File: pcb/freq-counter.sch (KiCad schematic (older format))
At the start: 52 parts, among them J1 RPM, J2 BNC, J3 for RPM, Q1 CSC388A, Q2 CSC388A, Q3 2SA1015, Q4 2SC1815, Q5 2SC1815, SW1 SW_SPDT, SW2 SW_Push, SW3 SW_Push, U1 SN74HC02N, U2 ATTINY4313-PU(freq-counter), U3 EE-SX460, Y1 10MHz

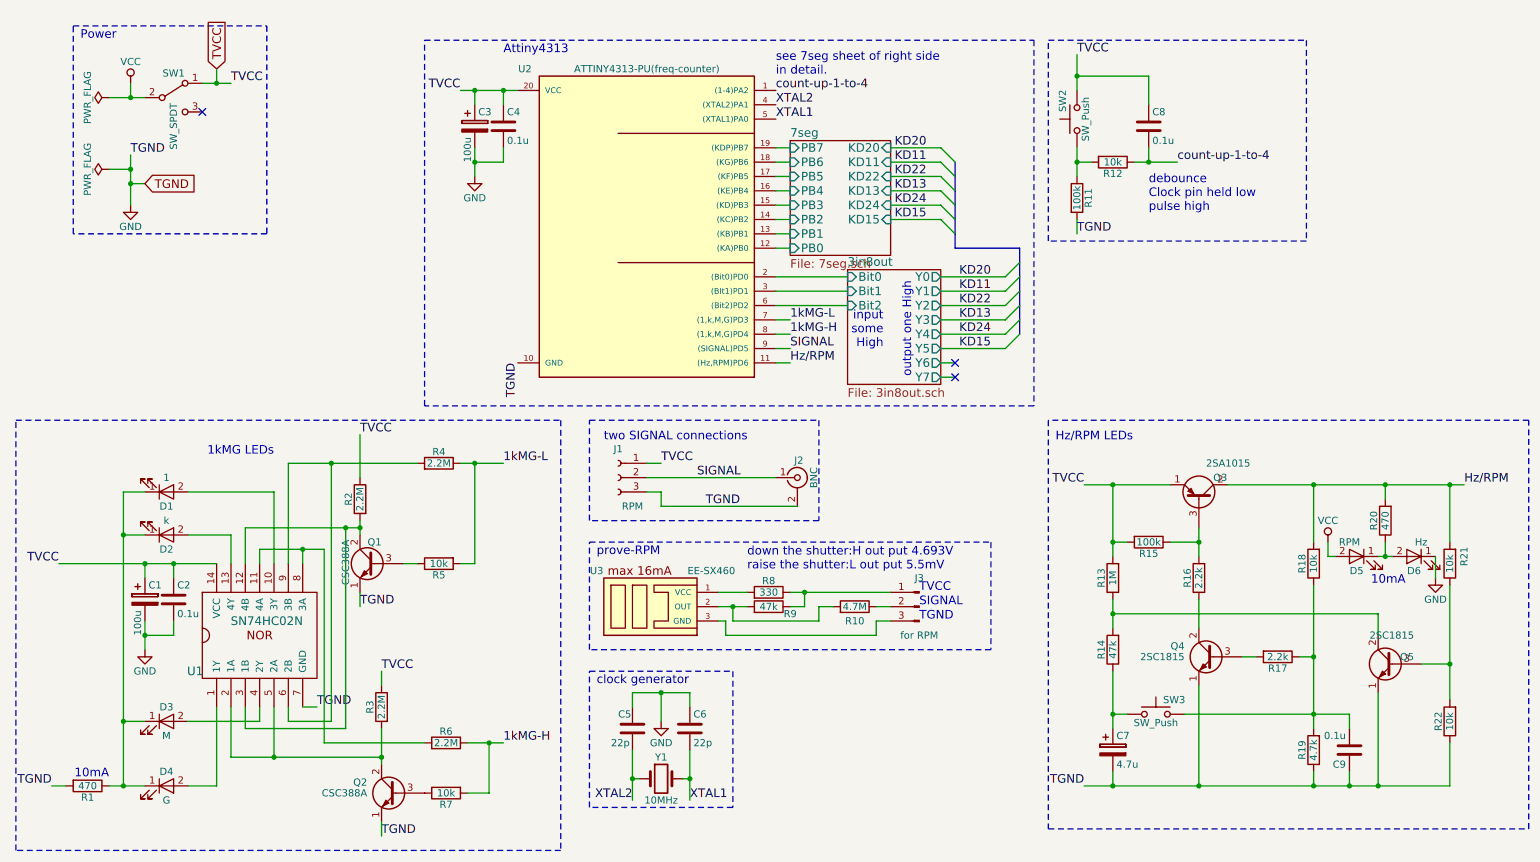
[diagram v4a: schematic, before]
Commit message: wire に未接続の設定をしていたら文句を言われたので，wireの未接続を削除。
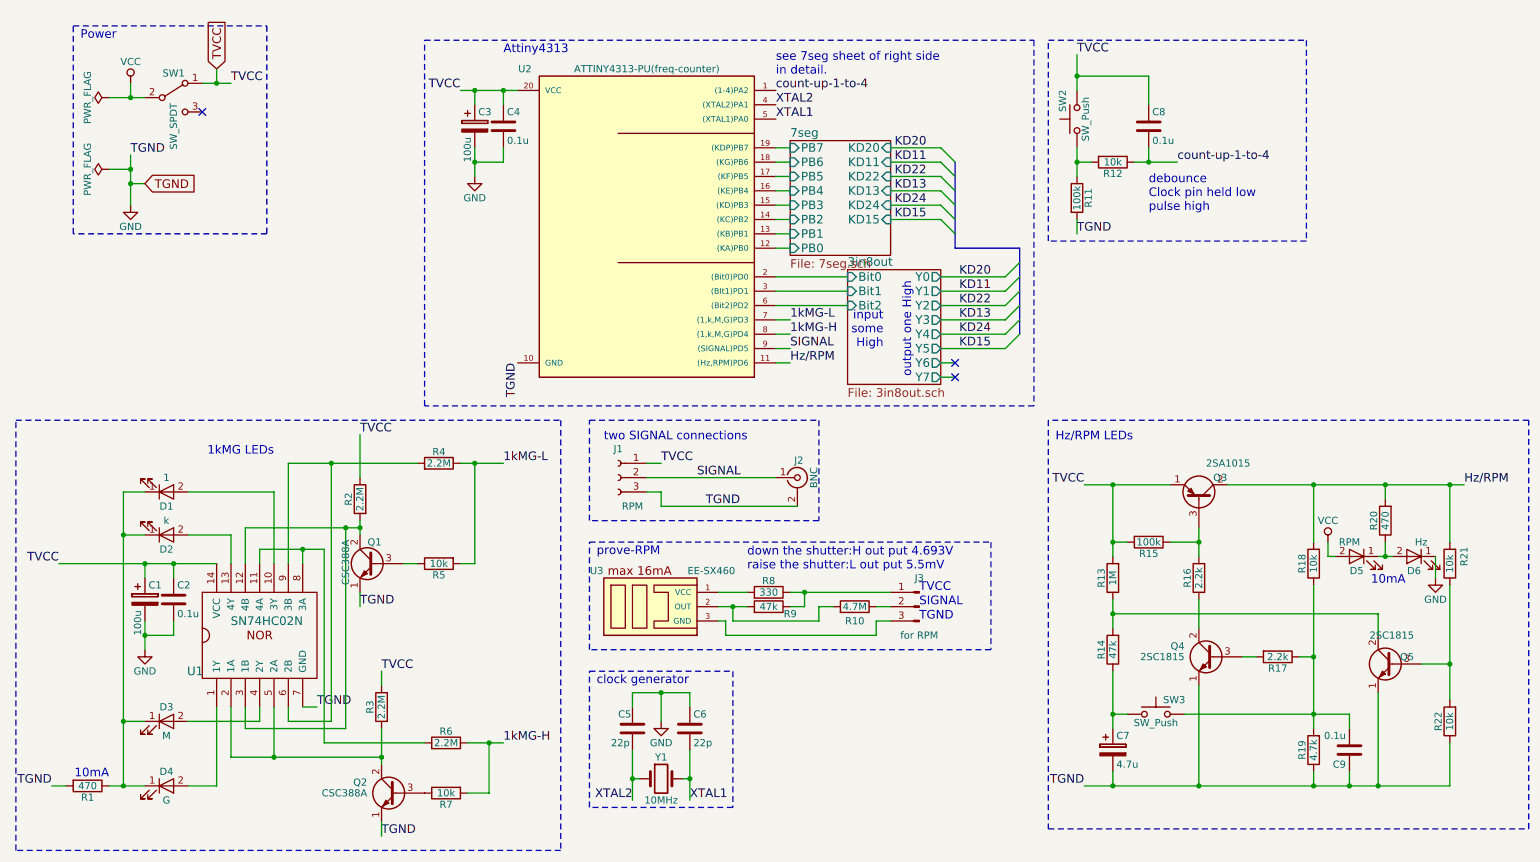
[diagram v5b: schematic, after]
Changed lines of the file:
@@
 $EndComp
 $Comp
-L VCC #PWR6
+L VCC #PWR01
 U 1 1 5A0DF4BD
 P 9700 4350
-F 0 "#PWR6" H 9700 4200 50  0001 C CNN
+F 0 "#PWR01" H 9700 4200 50  0001 C CNN
 F 1 "VCC" H 9700 4500 50  0000 C CNN
 F 2 "" H 9700 4350 50  0001 C CNN
@@
 $EndComp
 $Comp
-L GND #PWR7
+L GND #PWR02
 U 1 1 5A0DF6A9
 P 10450 4600
-F 0 "#PWR7" H 10450 4350 50  0001 C CNN
+F 0 "#PWR02" H 10450 4350 50  0001 C CNN
 F 1 "GND" H 10450 4450 50  0000 C CNN
 F 2 "" H 10450 4600 50  0001 C CNN
@@
 $EndComp
 $Comp
-L GND #PWR3
+L GND #PWR03
 U 1 1 5A10C10B
 P 1450 5100
-F 0 "#PWR3" H 1450 4850 50  0001 C CNN
+F 0 "#PWR03" H 1450 4850 50  0001 C CNN
 F 1 "GND" H 1450 4950 50  0000 C CNN
 F 2 "" H 1450 5100 50  0001 C CNN
@@
 $EndComp
 $Comp
-L GND #PWR5
+L GND #PWR04
 U 1 1 5A102C86
 P 5050 5600
-F 0 "#PWR5" H 5050 5350 50  0001 C CNN
+F 0 "#PWR04" H 5050 5350 50  0001 C CNN
 F 1 "GND" H 5050 5450 50  0000 C CNN
 F 2 "" H 5050 5600 50  0001 C CNN
@@
  down the shutter:H out put 4.693V\nraise the shutter:L out put 5.5mV
 Wire Wire Line
-	5950 4700 6050 4700
-Wire Wire Line
-	6050 4700 6650 4700
+	5950 4700 6650 4700
 Wire Wire Line
 	2050 4300 1750 4300
@@
 	2550 5500 2650 5500
 Wire Wire Line
-	850  4500 1450 4500
-Wire Wire Line
-	1450 4500 1650 4500
-Wire Wire Line
-	1650 4500 1950 4500
+	850  4500 1950 4500
 Wire Wire Line
 	2950 3900 2950 3600
 Wire Wire Line
-	2950 4200 2950 4250
-Wire Wire Line
-	2950 4250 2950 4300
+	2950 4200 2950 4300
 Wire Wire Line
 	2450 3800 2450 4500
 Wire Wire Line
-	2450 3800 2750 3800
-Wire Wire Line
-	2750 3800 3350 3800
+	2450 3800 3350 3800
 Connection ~ 3750 3800
 Wire Wire Line
@@
 Connection ~ 10100 4450
 Wire Wire Line
-	10050 4450 10100 4450
-Wire Wire Line
-	10100 4450 10150 4450
+	10050 4450 10150 4450
 Wire Wire Line
 	10100 4350 10100 4450
@@
 	10350 5200 10550 5200
 Wire Wire Line
-	10550 4650 10550 5200
-Wire Wire Line
-	10550 5200 10550 5450
-Wire Wire Line
-	9000 3950 9600 3950
-Wire Wire Line
-	9600 3950 10100 3950
-Wire Wire Line
-	10100 3950 10550 3950
-Wire Wire Line
-	10550 3950 10650 3950
+	10550 4650 10550 5450
+Wire Wire Line
+	9000 3950 10650 3950
 Wire Wire Line
 	9600 4350 9600 3950
@@
 	8300 5550 8200 5550
 Wire Wire Line
-	8200 5250 8200 5550
-Wire Wire Line
-	8200 5550 8200 5650
+	8200 5250 8200 5650
 Connection ~ 8200 3950
 Connection ~ 8200 4350
 Wire Wire Line
-	8000 3950 8200 3950
-Wire Wire Line
-	8200 3950 8600 3950
+	8000 3950 8600 3950
 Wire Wire Line
 	8200 4350 8300 4350
 Wire Wire Line
-	8200 3950 8200 4350
-Wire Wire Line
-	8200 4350 8200 4450
-Wire Wire Line
-	8200 4750 8200 4850
-Wire Wire Line
-	8200 4850 8200 4950
+	8200 3950 8200 4450
+Wire Wire Line
+	8200 4750 8200 4950
 Wire Wire Line
 	8800 4750 8800 4950
@@
 	8600 4350 8800 4350
 Wire Wire Line
-	8800 4250 8800 4350
-Wire Wire Line
-	8800 4350 8800 4450
-Wire Wire Line
-	8000 6050 8200 6050
-Wire Wire Line
-	8200 6050 8800 6050
-Wire Wire Line
-	8800 6050 9600 6050
-Wire Wire Line
-	9600 6050 9850 6050
-Wire Wire Line
-	9850 6050 10050 6050
-Wire Wire Line
-	10050 6050 10550 6050
+	8800 4250 8800 4450
+Wire Wire Line
+	8000 6050 10550 6050
 Wire Wire Line
 	9850 6050 9850 5950
 Connection ~ 9600 5550
 Wire Wire Line
-	8700 5550 9600 5550
-Wire Wire Line
-	9600 5550 9850 5550
+	8700 5550 9850 5550
 Wire Wire Line
 	9850 5550 9850 5650
@@
 	9500 5150 9600 5150
 Wire Wire Line
-	9600 4650 9600 5150
-Wire Wire Line
-	9600 5150 9600 5550
-Wire Wire Line
-	9600 5550 9600 5650
+	9600 4650 9600 5650
 Wire Notes Line
 	11100 3500 7750 3500
@@
 	8450 1300 8450 1100
 Wire Wire Line
-	7950 950  7950 1100
-Wire Wire Line
-	7950 1100 7950 1200
+	7950 950  7950 1200
 Connection ~ 8450 1700
 Wire Wire Line
 	8450 1700 8450 1600
 Wire Wire Line
-	8350 1700 8450 1700
-Wire Wire Line
-	8450 1700 8650 1700
+	8350 1700 8650 1700
 Connection ~ 7950 1700
 Wire Wire Line
 	8050 1700 7950 1700
 Wire Wire Line
-	7950 1600 7950 1700
-Wire Wire Line
-	7950 1700 7950 1800
+	7950 1600 7950 1800
 Wire Wire Line
 	3850 5750 3850 6100
 Wire Wire Line
-	1200 6050 1300 6050
-Wire Wire Line
-	1300 6050 1450 6050
+	1200 6050 1450 6050
 Wire Wire Line
 	1300 5600 1450 5600
@@
 Connection ~ 3850 5750
 Wire Wire Line
-	3700 5750 3850 5750
-Wire Wire Line
-	3850 5750 3950 5750
+	3700 5750 3950 5750
 Wire Wire Line
 	3350 4500 3250 4500
@@
 	3750 3800 3750 4500
 Wire Wire Line
-	3650 3800 3750 3800
-Wire Wire Line
-	3750 3800 3950 3800
+	3650 3800 3950 3800
 Wire Wire Line
 	3750 4500 3650 4500
 Wire Wire Line
-	3100 5650 3100 5850
-Wire Wire Line
-	3100 5850 3100 5900
+	3100 5650 3100 5900
 Wire Wire Line
 	2250 5500 2250 5600
@@
 	2950 4700 2950 4800
 Wire Wire Line
-	2150 4250 2850 4250
-Wire Wire Line
-	2850 4250 2950 4250
+	2150 4250 2950 4250
 Wire Wire Line
 	2850 5650 2850 4250
@@
 	2700 4400 2700 5750
 Wire Wire Line
-	2250 4400 2550 4400
-Wire Wire Line
-	2550 4400 2700 4400
+	2250 4400 2700 4400
 Wire Wire Line
 	2250 4400 2250 4500
@@
 	3100 5250 3100 5350
 Wire Wire Line
-	2050 5850 2350 5850
-Wire Wire Line
-	2350 5850 3100 5850
+	2050 5850 3100 5850
 Wire Wire Line
 	2350 5850 2350 5500
@@
 Connection ~ 1450 4500
 Wire Wire Line
-	1450 4900 1450 5000
-Wire Wire Line
-	1450 5000 1450 5100
+	1450 4900 1450 5100
 Wire Wire Line
 	1650 4500 1650 4600
@@
 	6650 1700 7000 1700
 Wire Bus Line
-	7100 1700 7100 1800
-Wire Bus Line
-	7100 1800 7100 1900
-Wire Bus Line
-	7100 1900 7100 2000
-Wire Bus Line
-	7100 2000 7100 2100
-Wire Bus Line
-	7100 2100 7100 2200
-Wire Bus Line
-	7100 2200 7100 2300
+	7100 1700 7100 2300
 Wire Wire Line
 	7000 2500 7450 2500
 Wire Bus Line
-	7550 2300 7550 2400
-Wire Bus Line
-	7550 2400 7550 2500
-Wire Bus Line
-	7550 2500 7550 2600
-Wire Bus Line
-	7550 2600 7550 2700
-Wire Bus Line
-	7550 2700 7550 2800
-Wire Bus Line
-	7550 2800 7550 2900
+	7550 2300 7550 2900
 Wire Bus Line
 	7100 2300 7550 2300
@@
 	4850 6000 4900 6000
 Wire Wire Line
-	4850 5800 4850 6000
-Wire Wire Line
-	4850 6000 4850 6150
+	4850 5800 4850 6150
 Wire Wire Line
 	4850 5500 4850 5400
 Wire Wire Line
-	4850 5400 5050 5400
-Wire Wire Line
-	5050 5400 5250 5400
+	4850 5400 5250 5400
 Wire Wire Line
 	5250 5400 5250 5500
@@
 	4550 6200 4550 5250
 Wire Wire Line
-	5250 5800 5250 6000
-Wire Wire Line
-	5250 6000 5250 6150
+	5250 5800 5250 6150
 Wire Wire Line
 	5450 4700 5650 4700
 Wire Wire Line
-	5450 4800 5550 4800
-Wire Wire Line
-	5550 4800 5650 4800
+	5450 4800 5650 4800
 Connection ~ 5550 4800
 Wire Notes Line
@@
 	6150 4800 6250 4800
 Wire Wire Line
-	1300 4000 1300 4300
-Wire Wire Line
-	1300 4300 1300 5600
-Wire Wire Line
-	1300 5600 1300 6050
+	1300 4000 1300 6050
 Connection ~ 1300 6050
 Connection ~ 1300 5600
@@
 $EndComp
 $Comp
-L VCC #PWR1
+L VCC #PWR05
 U 1 1 5A149A89
 P 1350 1150
-F 0 "#PWR1" H 1350 1000 50  0001 C CNN
+F 0 "#PWR05" H 1350 1000 50  0001 C CNN
 F 1 "VCC" H 1350 1300 50  0000 C CNN
 F 2 "" H 1350 1150 50  0001 C CNN
@@
 TVCC
 Wire Wire Line
-	3650 1200 3750 1200
-Wire Wire Line
-	3750 1200 3950 1200
-Wire Wire Line
-	3950 1200 4050 1200
-Wire Wire Line
-	1200 1250 1350 1250
-Wire Wire Line
-	1350 1250 1450 1250
+	3650 1200 4050 1200
+Wire Wire Line
+	1200 1250 1450 1250
 Wire Wire Line
 	1350 1250 1350 1150
 NoConn ~ 1850 1350
 $Comp
-L GND #PWR2
+L GND #PWR06
 U 1 1 5A14ACE7
 P 1350 2000
-F 0 "#PWR2" H 1350 1750 50  0001 C CNN
+F 0 "#PWR06" H 1350 1750 50  0001 C CNN
 F 1 "GND" H 1350 1850 50  0000 C CNN
 F 2 "" H 1350 2000 50  0001 C CNN
@@
 TGND
 Wire Wire Line
-	1350 1650 1350 1750
-Wire Wire Line
-	1350 1750 1350 1850
-Wire Wire Line
-	1350 1850 1350 2000
-$Comp
-L PWR_FLAG #FLG2
+	1350 1650 1350 2000
+$Comp
+L PWR_FLAG #FLG07
 U 1 1 5A14B084
 P 1200 1750
-F 0 "#FLG2" H 1200 1825 50  0001 C CNN
+F 0 "#FLG07" H 1200 1825 50  0001 C CNN
 F 1 "PWR_FLAG" H 1200 1900 50  0000 C CNN
 F 2 "" H 1200 1750 50  0001 C CNN
@@
 Connection ~ 1350 1750
 $Comp
-L PWR_FLAG #FLG1
+L PWR_FLAG #FLG08
 U 1 1 5A14B889
 P 1200 1250
-F 0 "#FLG1" H 1200 1325 50  0001 C CNN
+F 0 "#FLG08" H 1200 1325 50  0001 C CNN
 F 1 "PWR_FLAG" H 1200 1400 50  0000 C CNN
 F 2 "" H 1200 1250 50  0001 C CNN
@@
 $EndComp
 $Comp
-L GND #PWR4
+L GND #PWR09
 U 1 1 5A14CF4C
 P 3750 1800
-F 0 "#PWR4" H 3750 1550 50  0001 C CNN
+F 0 "#PWR09" H 3750 1550 50  0001 C CNN
 F 1 "GND" H 3750 1650 50  0000 C CNN
 F 2 "" H 3750 1800 50  0001 C CNN
@@
 	3750 1200 3750 1300
 Wire Wire Line
-	3750 1600 3750 1700
-Wire Wire Line
-	3750 1700 3750 1800
+	3750 1600 3750 1800
 Wire Wire Line
 	3950 1200 3950 1300
@@
 Power
 Wire Wire Line
-	1850 1150 1950 1150
-Wire Wire Line
-	1950 1150 2050 1150
+	1850 1150 2050 1150
 Text GLabel 1950 1050 1    60   Input ~ 0
 TVCC

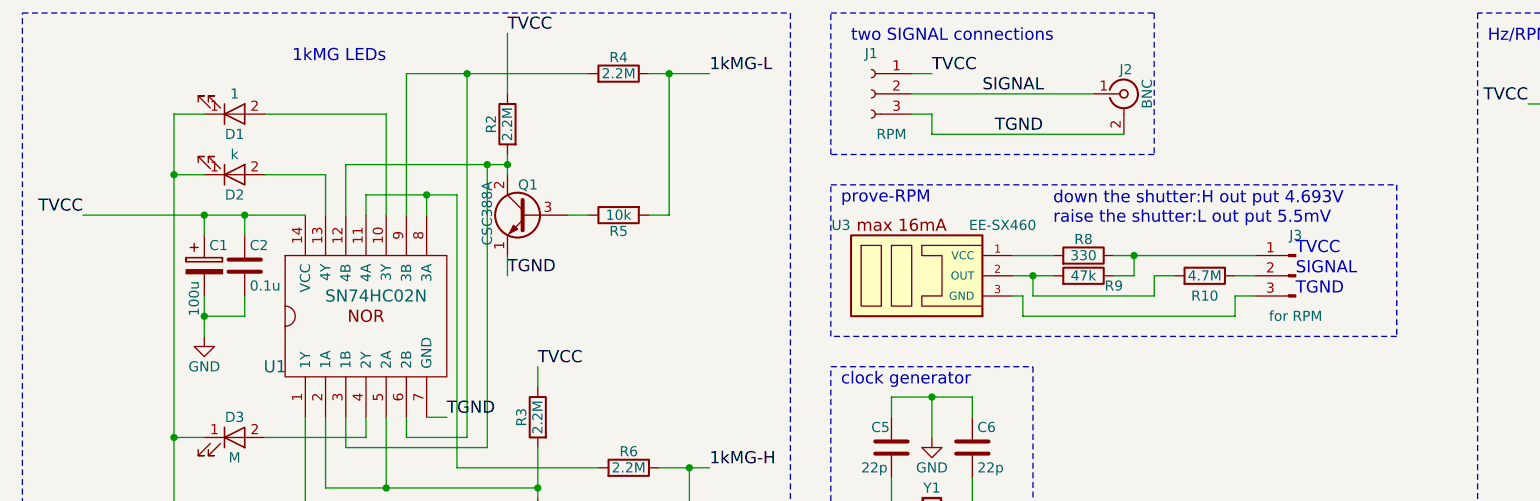
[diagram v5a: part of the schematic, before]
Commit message: 細々した配線誤りを修正。 fixed tiny mistake.
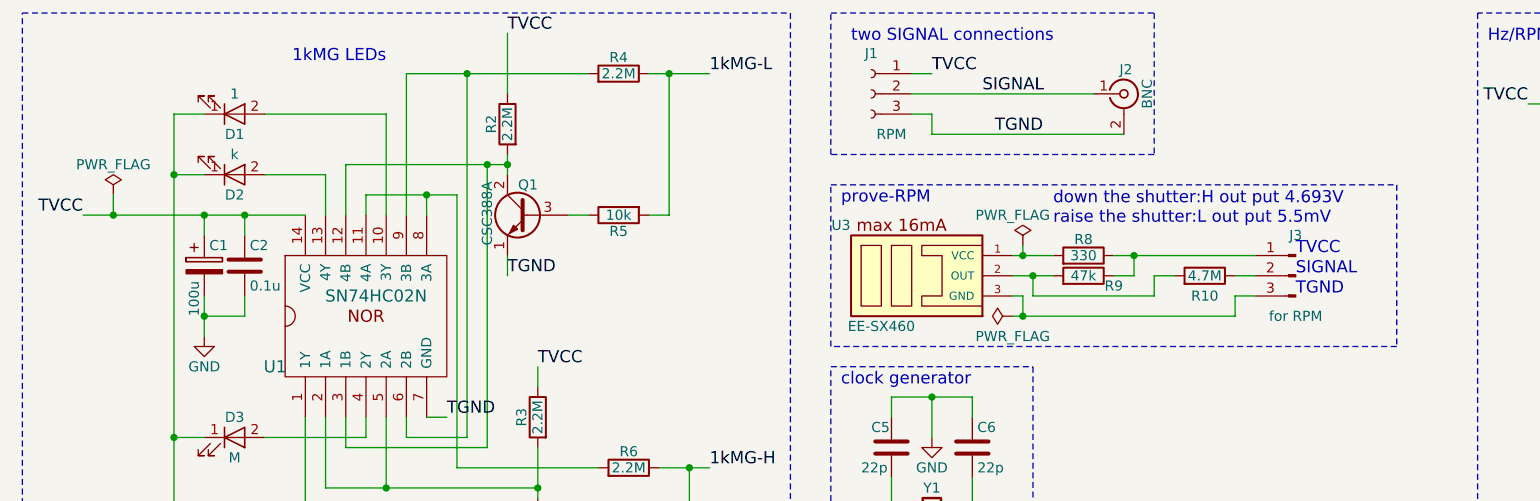
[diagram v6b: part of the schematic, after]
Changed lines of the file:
@@
 P 5050 4800
 F 0 "U3" H 4600 5050 50  0000 C CNN
-F 1 "EE-SX460" H 5400 5050 50  0000 C CNN
+F 1 "EE-SX460" H 4800 4550 50  0000 C CNN
 F 2 "3PIN_W30_D11_H8mm" H 5050 4500 50  0001 C CIN
 F 3 "" H 4700 4850 50  0001 C CNN
@@
 	4550 4350 7350 4350
 Wire Notes Line
-	7350 4350 7350 5100
-Wire Notes Line
-	7350 5100 4550 5100
-Wire Notes Line
-	4550 5100 4550 4350
+	7350 4350 7350 5150
+Wire Notes Line
+	7350 5150 4550 5150
+Wire Notes Line
+	4550 5150 4550 4350
 Wire Notes Line
 	4550 3500 6150 3500
@@
 	5500 4900 5500 5000
 Wire Wire Line
-	5500 5000 6550 5000
+	5450 5000 6550 5000
 Wire Wire Line
 	6550 5000 6550 4900
@@
 	1450 1850 1350 1850
 Connection ~ 1350 1850
+$Comp
+L PWR_FLAG #FLG010
+U 1 1 5A15C001
+P 1000 4400
+F 0 "#FLG010" H 1000 4475 50  0001 C CNN
+F 1 "PWR_FLAG" H 1000 4550 50  0000 C CNN
+F 2 "" H 1000 4400 50  0001 C CNN
+F 3 "" H 1000 4400 50  0001 C CNN
+	1    1000 4400
+	1    0    0    -1
+$EndComp
+Wire Wire Line
+	1000 4400 1000 4500
+Connection ~ 1000 4500
+$Comp
+L PWR_FLAG #FLG011
+U 1 1 5A15C58C
+P 5500 4650
+F 0 "#FLG011" H 5500 4725 50  0001 C CNN
+F 1 "PWR_FLAG" H 5450 4800 50  0000 C CNN
+F 2 "" H 5500 4650 50  0001 C CNN
+F 3 "" H 5500 4650 50  0001 C CNN
+	1    5500 4650
+	1    0    0    -1
+$EndComp
+Wire Wire Line
+	5500 4650 5500 4700
+Connection ~ 5500 4700
+$Comp
+L PWR_FLAG #FLG012
+U 1 1 5A15C934
+P 5450 5000
+F 0 "#FLG012" H 5450 5075 50  0001 C CNN
+F 1 "PWR_FLAG" V 5350 5000 50  0000 C CNN
+F 2 "" H 5450 5000 50  0001 C CNN
+F 3 "" H 5450 5000 50  0001 C CNN
+	1    5450 5000
+	0    -1   -1   0
+$EndComp
+Connection ~ 5500 5000
 $EndSCHEMATC
